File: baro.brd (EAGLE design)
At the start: 20.6 x 19 mm, 7 parts, among them IC1 MPL3115A2

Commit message: minor mods
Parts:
- moved C1 2.23 mm to (13.9, 8.89), turned to 180 degrees
- moved R1 1.30 mm to (7.86, 5.45)
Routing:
- net VCC: track 29.1 -> 24.3 mm
- net GND: track 27.5 -> 27.0 mm
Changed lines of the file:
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@@
 <wire x1="18.6" y1="19" x2="-2" y2="19" width="0" layer="20"/>
 <wire x1="-2" y1="19" x2="-2" y2="0" width="0" layer="20"/>
-<hole x="15.5" y="16.1" drill="3.2"/>
+<hole x="15.2" y="16" drill="3.2"/>
 <wire x1="2.4" y1="21.3" x2="2.4" y2="-1.5" width="0.4064" layer="48"/>
 <text x="2.1" y="-5.4" size="1.778" layer="48" rot="R90">absägen für onboardmodul</text>
@@
 <elements>
 <element name="IC1" library="seb" package="LGA8" value="MPL3115A2" x="10.14" y="11.62" rot="R180"/>
-<element name="C1" library="SparkFun-Passives" package="0805" value="" x="15.21" y="10.66" rot="R270"/>
+<element name="C1" library="SparkFun-Passives" package="0805" value="" x="13.86" y="8.89" rot="R180"/>
 <element name="C3" library="SparkFun-Passives" package="0805" value="" x="13.36" y="11.74" rot="R270"/>
-<element name="R1" library="SparkFun-Passives" package="0805" value="" x="8.56" y="6.55" rot="R270"/>
+<element name="R1" library="SparkFun-Passives" package="0805" value="" x="7.86" y="5.45" rot="R270"/>
 <element name="R2" library="SparkFun-Passives" package="0805" value="" x="5.76" y="8.76" rot="R270"/>
 <element name="C2" library="rcl" package="SMC_C" value="" x="13.49" y="4.58"/>
@@
 <contactref element="JP1" pad="1"/>
 <wire x1="2.57" y1="2.06" x2="2.73" y2="1.9" width="0.4064" layer="1"/>
-<wire x1="11.14" y1="12.245" x2="12.965" y2="12.245" width="0.4064" layer="1"/>
-<wire x1="12.965" y1="12.245" x2="13.36" y2="12.64" width="0.4064" layer="1"/>
+<wire x1="11.14" y1="12.245" x2="12.2" y2="12.3" width="0.4064" layer="1"/>
+<wire x1="12.2" y1="12.3" x2="12.665" y2="12.645" width="0.4064" layer="1"/>
+<wire x1="12.665" y1="12.645" x2="13.36" y2="12.64" width="0.4064" layer="1"/>
 <wire x1="13.36" y1="12.64" x2="14.13" y2="12.64" width="0.4064" layer="1"/>
-<wire x1="14.13" y1="12.64" x2="15.21" y2="11.56" width="0.4064" layer="1"/>
-<wire x1="15.99" y1="4.58" x2="15.99" y2="5.89" width="0.4064" layer="1"/>
-<wire x1="15.99" y1="5.89" x2="17" y2="6.9" width="0.4064" layer="1"/>
-<wire x1="17" y1="6.9" x2="17" y2="9.77" width="0.4064" layer="1"/>
-<wire x1="17" y1="9.77" x2="15.21" y2="11.56" width="0.4064" layer="1"/>
-<wire x1="2.57" y1="2.06" x2="13.47" y2="2.06" width="0.4064" layer="1"/>
-<wire x1="13.47" y1="2.06" x2="15.99" y2="4.58" width="0.4064" layer="1"/>
+<wire x1="2.57" y1="2.06" x2="14.37" y2="2.06" width="0.4064" layer="1"/>
+<wire x1="14.37" y1="2.06" x2="15.99" y2="4.58" width="0.4064" layer="1"/>
+<wire x1="14.13" y1="12.64" x2="14.76" y2="12.01" width="0.4064" layer="1"/>
+<wire x1="14.76" y1="12.01" x2="14.76" y2="8.89" width="0.4064" layer="1"/>
+<wire x1="14.76" y1="8.89" x2="15.99" y2="7.66" width="0.4064" layer="1"/>
+<wire x1="15.99" y1="7.66" x2="15.99" y2="4.58" width="0.4064" layer="1"/>
 </signal>
 <signal name="VCC">
@@
 <contactref element="R2" pad="2"/>
 <contactref element="JP1" pad="2"/>
-<wire x1="2.57" y1="4.6" x2="5.8" y2="4.6" width="0.4064" layer="1"/>
-<wire x1="5.8" y1="4.6" x2="8.1" y2="4.6" width="0.4064" layer="1"/>
-<wire x1="8.1" y1="4.6" x2="8.6" y2="4.6" width="0.4064" layer="1"/>
-<wire x1="5.76" y1="7.86" x2="5.76" y2="4.64" width="0.4064" layer="1"/>
-<wire x1="5.76" y1="4.64" x2="5.8" y2="4.6" width="0.4064" layer="1"/>
-<wire x1="8.56" y1="5.65" x2="8.56" y2="4.64" width="0.4064" layer="1"/>
-<wire x1="8.56" y1="4.64" x2="8.6" y2="4.6" width="0.4064" layer="1"/>
 <wire x1="11.14" y1="13.495" x2="10.695" y2="13.495" width="0.4064" layer="1"/>
-<wire x1="10.695" y1="13.495" x2="10.2" y2="13" width="0.4064" layer="1"/>
-<wire x1="10.2" y1="13" x2="10.2" y2="10.685" width="0.4064" layer="1"/>
-<wire x1="10.2" y1="10.685" x2="11.14" y2="9.745" width="0.4064" layer="1"/>
-<wire x1="11.14" y1="9.745" x2="15.195" y2="9.745" width="0.4064" layer="1"/>
-<wire x1="15.195" y1="9.745" x2="15.21" y2="9.76" width="0.4064" layer="1"/>
-<wire x1="15.21" y1="9.76" x2="15.21" y2="8.8" width="0.4064" layer="1"/>
-<wire x1="15.21" y1="8.8" x2="10.99" y2="4.58" width="0.4064" layer="1"/>
-<wire x1="10.99" y1="4.58" x2="8.12" y2="4.58" width="0.4064" layer="1"/>
-<wire x1="8.12" y1="4.58" x2="8.1" y2="4.6" width="0.4064" layer="1"/>
+<wire x1="10.695" y1="13.495" x2="10.2" y2="12.8" width="0.4064" layer="1"/>
+<wire x1="10.2" y1="12.8" x2="10.2" y2="10.485" width="0.4064" layer="1"/>
+<wire x1="10.2" y1="10.485" x2="11.14" y2="9.745" width="0.4064" layer="1"/>
+<wire x1="2.57" y1="4.6" x2="2.59" y2="4.58" width="0.4064" layer="1"/>
+<wire x1="2.59" y1="4.58" x2="5.7" y2="4.58" width="0.4064" layer="1"/>
+<wire x1="7.83" y1="4.58" x2="10.99" y2="4.58" width="0.4064" layer="1"/>
+<wire x1="5.76" y1="7.86" x2="5.7" y2="7.8" width="0.4064" layer="1"/>
+<wire x1="5.7" y1="7.8" x2="5.7" y2="4.58" width="0.4064" layer="1"/>
+<wire x1="7.86" y1="4.55" x2="7.83" y2="4.58" width="0.4064" layer="1"/>
+<wire x1="7.83" y1="4.58" x2="5.7" y2="4.58" width="0.4064" layer="1"/>
+<wire x1="10.99" y1="4.58" x2="12.9" y2="6.49" width="0.4064" layer="1"/>
+<wire x1="12.9" y1="6.49" x2="12.9" y2="8.95" width="0.4064" layer="1"/>
+<wire x1="12.9" y1="9.2" x2="12.9" y2="9.6" width="0.4064" layer="1"/>
+<wire x1="12.9" y1="9.6" x2="12.755" y2="9.745" width="0.4064" layer="1"/>
+<wire x1="12.755" y1="9.745" x2="11.14" y2="9.745" width="0.4064" layer="1"/>
+<wire x1="12.96" y1="8.89" x2="12.9" y2="8.95" width="0.4064" layer="1"/>
+<wire x1="12.9" y1="8.95" x2="12.9" y2="9.2" width="0.4064" layer="1"/>
 </signal>
 <signal name="SCL">
@@
 <contactref element="R1" pad="1"/>
 <contactref element="JP1" pad="3"/>
-<wire x1="9.14" y1="9.745" x2="8.5" y2="9.745" width="0.4064" layer="1"/>
-<wire x1="8.5" y1="9.745" x2="7.545" y2="9.745" width="0.4064" layer="1"/>
-<wire x1="7.545" y1="9.745" x2="6.6" y2="8.8" width="0.4064" layer="1"/>
-<wire x1="6.6" y1="8.8" x2="4.23" y2="8.8" width="0.4064" layer="1"/>
-<wire x1="4.23" y1="8.8" x2="2.57" y2="7.14" width="0.4064" layer="1"/>
-<wire x1="8.56" y1="7.45" x2="8.56" y2="9.685" width="0.4064" layer="1"/>
-<wire x1="8.56" y1="9.685" x2="8.5" y2="9.745" width="0.4064" layer="1"/>
+<wire x1="9.14" y1="9.745" x2="7.745" y2="9.745" width="0.4064" layer="1"/>
+<wire x1="7.745" y1="9.745" x2="6.8" y2="8.8" width="0.4064" layer="1"/>
+<wire x1="6.8" y1="8.8" x2="4.73" y2="8.8" width="0.4064" layer="1"/>
+<wire x1="4.73" y1="8.8" x2="2.57" y2="7.14" width="0.4064" layer="1"/>
+<wire x1="7.86" y1="6.35" x2="7.86" y2="7.74" width="0.4064" layer="1"/>
+<wire x1="7.86" y1="7.74" x2="6.8" y2="8.8" width="0.4064" layer="1"/>
 </signal>
 <signal name="SDA">

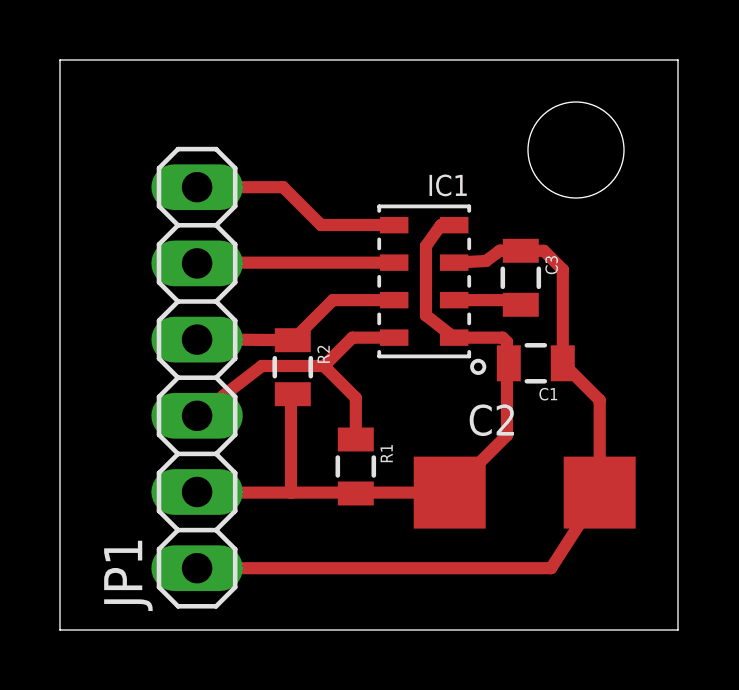
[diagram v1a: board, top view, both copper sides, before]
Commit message: rundung wegen hf abstrahlung.... und weils geht
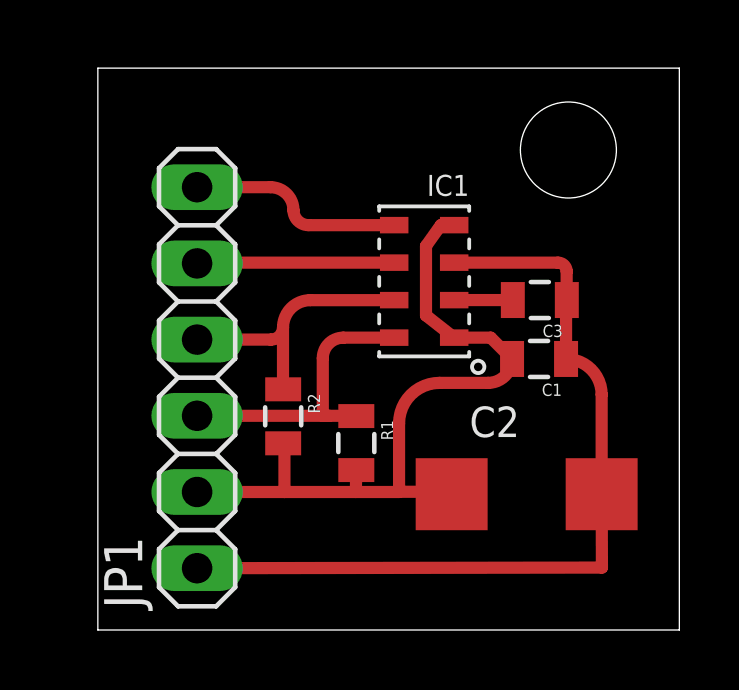
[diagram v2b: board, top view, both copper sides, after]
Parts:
- moved R2 1.67 mm to (5.44, 7.12)
- moved C3 0.98 mm to (14.0, 11.0), turned to 180 degrees
- moved R1 0.78 mm to (7.88, 6.23)
- moved C1 0.18 mm to (14.0, 9.03)
- moved C2 0.08 mm to (13.6, 4.53)
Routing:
- net SDA: track 7.12 -> 9.18 mm
- net GND: track 27.0 -> 28.0 mm
- net VCC: track 24.3 -> 24.9 mm
- net SCL: track 10.4 -> 9.90 mm
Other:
- board size 20.6 x 19 mm -> 19.4 x 18.7 mm
